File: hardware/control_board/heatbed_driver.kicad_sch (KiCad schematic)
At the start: 12 parts, among them J1 Conn_01x01, J2 Conn_01x01, Q2 IRF1018ESTRLPBF, U8 TLP183

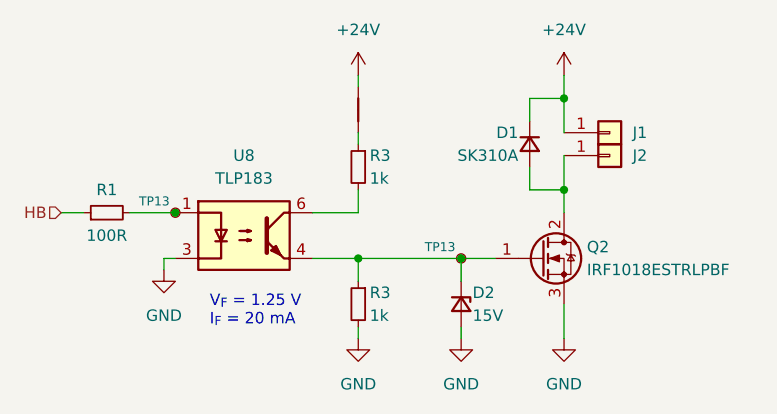
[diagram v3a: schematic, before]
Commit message: Use Schottky flyback diode for heatbed
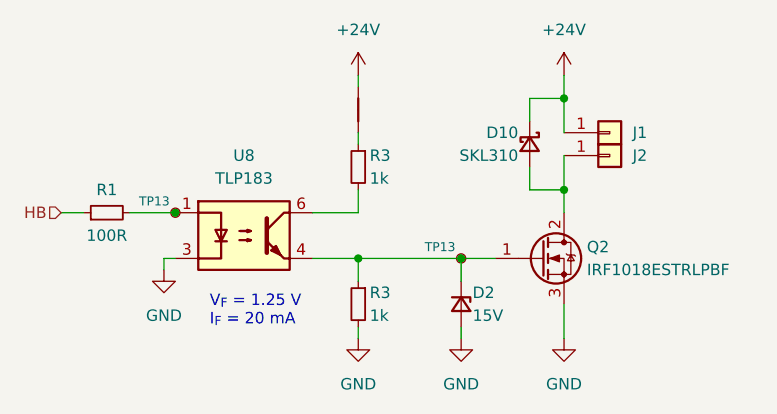
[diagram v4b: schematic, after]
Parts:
- removed D1: SK310A, Diode_SMD:D_SMA, symbol Device:D_Small
- added D10: SKL310, Diode_SMD:D_SOD-123F, symbol Device:D_Schottky_Small
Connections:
- net +24V: now also D10.1 (K)
- net at J2.1 (Pin_1), Q2.2 (D): now also D10.2 (A)
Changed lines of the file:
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@@
   (title_block
     (title "Heatbed Driver")
-    (date "2023-11-13")
+    (date "2023-11-14")
     (rev "${REVISION}")
     (company "Author: I. Kajdan")
@@
     )
   )
+  (symbol (lib_id "Device:D_Schottky_Small") (at 166.37 92.71 270) (unit 1)
+    (in_bom yes) (on_board yes) (dnp no)
+    (property "Reference" "D10" (at 165.1 91.44 90)
+      (effects (font (size 1.27 1.27)) (justify right))
+    )
+    (property "Value" "SKL310" (at 165.1 93.98 90)
+      (effects (font (size 1.27 1.27)) (justify right))
+    )
+    (property "Footprint" "Diode_SMD:D_SOD-123F" (at 166.37 92.71 90)
+      (effects (font (size 1.27 1.27)) hide)
+    )
+    (property "Datasheet" "https://www.mouser.pl/datasheet/2/849/skl32-3324186.pdf" (at 166.37 92.71 90)
+      (effects (font (size 1.27 1.27)) hide)
+    )
+    (pin "1")
+    (pin "2")
+    (instances
+      (project "control_board"
+        (path "/b652b05a-4e3d-4ad1-b032-18886abe7d45/d341d3a2-ea4e-4772-851c-7c5b5be32855"
+          (reference "D10") (unit 1)
+        )
+      )
+    )
+  )
   (symbol (lib_id "Connector_Generic:Conn_01x01") (at 175.26 91.44 0) (mirror x) (unit 1)
     (in_bom no) (on_board yes) (dnp no)
@@
         )
       )
-    )
-  )
-  (symbol (lib_id "Device:D_Small") (at 166.37 92.71 90) (mirror x) (unit 1)
-    (in_bom yes) (on_board yes) (dnp no)
-    (property "Reference" "D1" (at 165.1 91.44 90)
-      (effects (font (size 1.27 1.27)) (justify left))
-    )
-    (property "Value" "SK310A" (at 165.1 93.98 90)
-      (effects (font (size 1.27 1.27)) (justify left))
-    )
-    (property "Footprint" "Diode_SMD:D_SMA" (at 166.37 92.71 90)
-      (effects (font (size 1.27 1.27)) hide)
-    )
-    (property "Datasheet" "https://www.smc-diodes.com/propdf/SK310A%20N0945%20REV.A.pdf" (at 166.37 92.71 90)
-      (effects (font (size 1.27 1.27)) hide)
-    )
-    (pin "1")
-    (pin "2")
-    (instances
-      (project "control_board"
-        (path "/82fde900-07e6-41de-9b57-509c777c8289"
-          (reference "D1") (unit 1)
-        )
-      )
-      (project "control_board"
-        (path "/b652b05a-4e3d-4ad1-b032-18886abe7d45"
-          (reference "D1") (unit 1)
-        )
-        (path "/b652b05a-4e3d-4ad1-b032-18886abe7d45/d341d3a2-ea4e-4772-851c-7c5b5be32855"
-          (reference "D10") (unit 1)
-        )
-      )

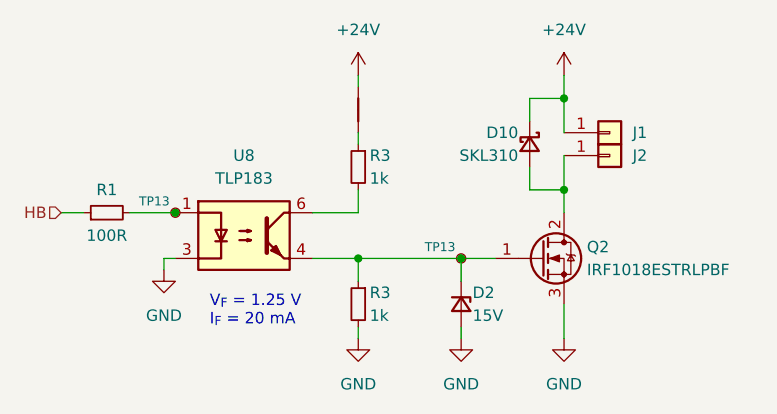
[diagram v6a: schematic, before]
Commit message: Update reference designators
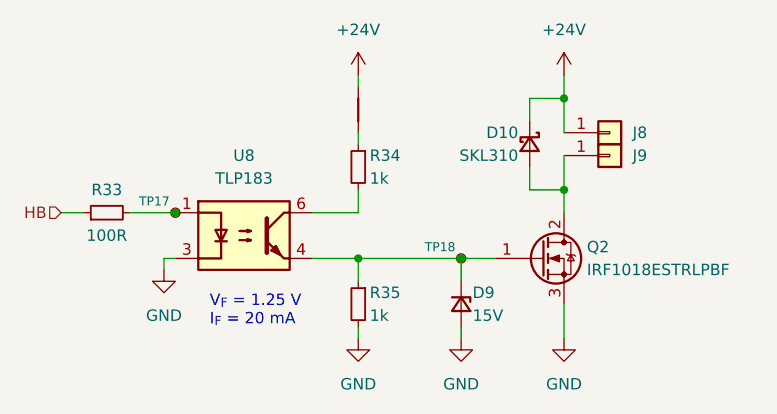
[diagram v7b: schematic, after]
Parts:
- renumbered D2 to D9, J1 to J8, J2 to J9, R1 to R33, R3 to R34, R3 to R35, TP13 to TP17, TP13 to TP18
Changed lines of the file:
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@@
   (symbol (lib_id "Connector:TestPoint_Small") (at 127 100.33 0) (unit 1)
     (in_bom no) (on_board yes) (dnp no)
-    (property "Reference" "TP13" (at 126.365 99.06 0)
+    (property "Reference" "TP17" (at 126.365 99.06 0)
       (effects (font (size 1 1)) (justify right))
     )
@@
     (instances
       (project "control_board"
-        (path "/b652b05a-4e3d-4ad1-b032-18886abe7d45/02711725-e382-48ba-bf33-23fe46c66e66"
-          (reference "TP13") (unit 1)
-        )
         (path "/b652b05a-4e3d-4ad1-b032-18886abe7d45/d341d3a2-ea4e-4772-851c-7c5b5be32855"
           (reference "TP17") (unit 1)
@@
   (symbol (lib_id "Connector_Generic:Conn_01x01") (at 175.26 91.44 0) (mirror x) (unit 1)
     (in_bom no) (on_board yes) (dnp no)
-    (property "Reference" "J1" (at 177.8 91.44 0)
+    (property "Reference" "J8" (at 177.8 91.44 0)
       (effects (font (size 1.27 1.27)) (justify left))
     )
@@
     (instances
       (project "control_board"
-        (path "/b652b05a-4e3d-4ad1-b032-18886abe7d45"
-          (reference "J1") (unit 1)
-        )
         (path "/b652b05a-4e3d-4ad1-b032-18886abe7d45/d341d3a2-ea4e-4772-851c-7c5b5be32855"
           (reference "J8") (unit 1)
@@
   (symbol (lib_id "power:GND") (at 125.73 106.68 0) (unit 1)
     (in_bom yes) (on_board yes) (dnp no)
-    (property "Reference" "#PWR08" (at 125.73 113.03 0)
+    (property "Reference" "#PWR077" (at 125.73 113.03 0)
       (effects (font (size 1.27 1.27)) hide)
     )
@@
     (instances
       (project "control_board"
-        (path "/82fde900-07e6-41de-9b57-509c777c8289"
-          (reference "#PWR08") (unit 1)
-        )
-      )
-      (project "control_board"
-        (path "/b652b05a-4e3d-4ad1-b032-18886abe7d45"
-          (reference "#PWR01") (unit 1)
-        )
         (path "/b652b05a-4e3d-4ad1-b032-18886abe7d45/d341d3a2-ea4e-4772-851c-7c5b5be32855"
           (reference "#PWR077") (unit 1)
@@
   (symbol (lib_id "power:GND") (at 158.75 114.3 0) (unit 1)
     (in_bom yes) (on_board yes) (dnp no)
-    (property "Reference" "#PWR078" (at 158.75 120.65 0)
+    (property "Reference" "#PWR080" (at 158.75 120.65 0)
       (effects (font (size 1.27 1.27)) hide)
     )
@@
     (instances
       (project "control_board"
-        (path "/b652b05a-4e3d-4ad1-b032-18886abe7d45/6b868c6a-e629-4d3b-add8-74bb26b34401"
-          (reference "#PWR078") (unit 1)
-        )
         (path "/b652b05a-4e3d-4ad1-b032-18886abe7d45/d341d3a2-ea4e-4772-851c-7c5b5be32855"
           (reference "#PWR080") (unit 1)
@@
   (symbol (lib_id "power:+24V") (at 170.18 85.09 0) (unit 1)
     (in_bom yes) (on_board yes) (dnp no)
-    (property "Reference" "#PWR05" (at 170.18 88.9 0)
+    (property "Reference" "#PWR081" (at 170.18 88.9 0)
       (effects (font (size 1.27 1.27)) hide)
     )
@@
     (instances
       (project "control_board"
-        (path "/82fde900-07e6-41de-9b57-509c777c8289"
-          (reference "#PWR05") (unit 1)
-        )
-      )
-      (project "control_board"
-        (path "/b652b05a-4e3d-4ad1-b032-18886abe7d45"
-          (reference "#PWR012") (unit 1)
-        )
         (path "/b652b05a-4e3d-4ad1-b032-18886abe7d45/d341d3a2-ea4e-4772-851c-7c5b5be32855"
           (reference "#PWR081") (unit 1)
@@
   (symbol (lib_id "Device:R_Small") (at 119.38 100.33 90) (unit 1)
     (in_bom yes) (on_board yes) (dnp no)
-    (property "Reference" "R1" (at 119.38 97.79 90)
+    (property "Reference" "R33" (at 119.38 97.79 90)
       (effects (font (size 1.27 1.27)))
     )
@@
     (instances
       (project "control_board"
-        (path "/82fde900-07e6-41de-9b57-509c777c8289"
-          (reference "R1") (unit 1)
-        )
-      )
-      (project "control_board"
-        (path "/b652b05a-4e3d-4ad1-b032-18886abe7d45"
-          (reference "R1") (unit 1)
-        )
         (path "/b652b05a-4e3d-4ad1-b032-18886abe7d45/d341d3a2-ea4e-4772-851c-7c5b5be32855"
           (reference "R33") (unit 1)
@@
   (symbol (lib_id "Device:R_Small") (at 147.32 95.25 0) (mirror y) (unit 1)
     (in_bom yes) (on_board yes) (dnp no)
-    (property "Reference" "R3" (at 148.59 93.98 0)
+    (property "Reference" "R34" (at 148.59 93.98 0)
       (effects (font (size 1.27 1.27)) (justify right))
     )
@@
     (instances
       (project "control_board"
-        (path "/82fde900-07e6-41de-9b57-509c777c8289"
-          (reference "R3") (unit 1)
-        )
-      )
-      (project "control_board"
-        (path "/b652b05a-4e3d-4ad1-b032-18886abe7d45"
-          (reference "R3") (unit 1)
-        )
         (path "/b652b05a-4e3d-4ad1-b032-18886abe7d45/d341d3a2-ea4e-4772-851c-7c5b5be32855"
           (reference "R34") (unit 1)
@@
   (symbol (lib_id "Device:D_Zener_Small") (at 158.75 110.49 270) (unit 1)
     (in_bom yes) (on_board yes) (dnp no)
-    (property "Reference" "D2" (at 160.02 109.22 90)
+    (property "Reference" "D9" (at 160.02 109.22 90)
       (effects (font (size 1.27 1.27)) (justify left))
     )
@@
     (instances
       (project "control_board"
-        (path "/b652b05a-4e3d-4ad1-b032-18886abe7d45/6b868c6a-e629-4d3b-add8-74bb26b34401"
-          (reference "D2") (unit 1)
-        )
         (path "/b652b05a-4e3d-4ad1-b032-18886abe7d45/d341d3a2-ea4e-4772-851c-7c5b5be32855"
           (reference "D9") (unit 1)
@@
   (symbol (lib_id "power:GND") (at 147.32 114.3 0) (unit 1)
     (in_bom yes) (on_board yes) (dnp no)
-    (property "Reference" "#PWR078" (at 147.32 120.65 0)
+    (property "Reference" "#PWR079" (at 147.32 120.65 0)
       (effects (font (size 1.27 1.27)) hide)
     )
@@
     (instances
       (project "control_board"
-        (path "/b652b05a-4e3d-4ad1-b032-18886abe7d45/6b868c6a-e629-4d3b-add8-74bb26b34401"
-          (reference "#PWR078") (unit 1)
-        )
         (path "/b652b05a-4e3d-4ad1-b032-18886abe7d45/d341d3a2-ea4e-4772-851c-7c5b5be32855"
           (reference "#PWR079") (unit 1)
@@
   (symbol (lib_id "Device:R_Small") (at 147.32 110.49 0) (mirror y) (unit 1)
     (in_bom yes) (on_board yes) (dnp no)
-    (property "Reference" "R3" (at 148.59 109.22 0)
+    (property "Reference" "R35" (at 148.59 109.22 0)
       (effects (font (size 1.27 1.27)) (justify right))
     )
@@
     (instances
       (project "control_board"
-        (path "/82fde900-07e6-41de-9b57-509c777c8289"
-          (reference "R3") (unit 1)
-        )
-      )
-      (project "control_board"
-        (path "/b652b05a-4e3d-4ad1-b032-18886abe7d45"
-          (reference "R3") (unit 1)
-        )
         (path "/b652b05a-4e3d-4ad1-b032-18886abe7d45/d341d3a2-ea4e-4772-851c-7c5b5be32855"
           (reference "R35") (unit 1)
@@
   (symbol (lib_id "power:GND") (at 170.18 114.3 0) (unit 1)
     (in_bom yes) (on_board yes) (dnp no)
-    (property "Reference" "#PWR078" (at 170.18 120.65 0)
+    (property "Reference" "#PWR082" (at 170.18 120.65 0)
       (effects (font (size 1.27 1.27)) hide)
     )
@@
     (instances
       (project "control_board"
-        (path "/b652b05a-4e3d-4ad1-b032-18886abe7d45/6b868c6a-e629-4d3b-add8-74bb26b34401"
-          (reference "#PWR078") (unit 1)
-        )
         (path "/b652b05a-4e3d-4ad1-b032-18886abe7d45/d341d3a2-ea4e-4772-851c-7c5b5be32855"
           (reference "#PWR082") (unit 1)
@@
   (symbol (lib_id "Connector_Generic:Conn_01x01") (at 175.26 93.98 0) (unit 1)
     (in_bom no) (on_board yes) (dnp no)
-    (property "Reference" "J2" (at 177.8 93.98 0)
+    (property "Reference" "J9" (at 177.8 93.98 0)
       (effects (font (size 1.27 1.27)) (justify left))
     )
@@
     (instances
       (project "control_board"
-        (path "/b652b05a-4e3d-4ad1-b032-18886abe7d45"
-          (reference "J2") (unit 1)
-        )
         (path "/b652b05a-4e3d-4ad1-b032-18886abe7d45/d341d3a2-ea4e-4772-851c-7c5b5be32855"
           (reference "J9") (unit 1)
@@
   (symbol (lib_id "Connector:TestPoint_Small") (at 158.75 105.41 0) (unit 1)
     (in_bom no) (on_board yes) (dnp no)
-    (property "Reference" "TP13" (at 158.115 104.14 0)
+    (property "Reference" "TP18" (at 158.115 104.14 0)
       (effects (font (size 1 1)) (justify right))
     )
@@
     (instances
       (project "control_board"
-        (path "/b652b05a-4e3d-4ad1-b032-18886abe7d45/02711725-e382-48ba-bf33-23fe46c66e66"
-          (reference "TP13") (unit 1)
-        )
         (path "/b652b05a-4e3d-4ad1-b032-18886abe7d45/d341d3a2-ea4e-4772-851c-7c5b5be32855"
           (reference "TP18") (unit 1)
@@
   (symbol (lib_id "power:+24V") (at 147.32 85.09 0) (unit 1)
     (in_bom yes) (on_board yes) (dnp no)
-    (property "Reference" "#PWR06" (at 147.32 88.9 0)
+    (property "Reference" "#PWR078" (at 147.32 88.9 0)
       (effects (font (size 1.27 1.27)) hide)
     )
@@
     (instances
       (project "control_board"
-        (path "/82fde900-07e6-41de-9b57-509c777c8289"
-          (reference "#PWR06") (unit 1)
-        )
-      )
-      (project "control_board"
-        (path "/b652b05a-4e3d-4ad1-b032-18886abe7d45"
-          (reference "#PWR06") (unit 1)
-        )
         (path "/b652b05a-4e3d-4ad1-b032-18886abe7d45/d341d3a2-ea4e-4772-851c-7c5b5be32855"
           (reference "#PWR078") (unit 1)
